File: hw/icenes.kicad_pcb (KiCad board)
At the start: 6 copper layers, 206 parts, among them J1 USB_B_Micro, J2 Barrel_Jack_Switch, J3 Conn_02x11_Odd_Even, J4 Conn_02x31_Odd_Even, J5 Conn_02x31_Odd_Even, J6 NES-Connector-72pin, U1 TPS62050, U10 74ALVC164245, U11 74ALVC164245, U12 74ALVC164245, U13 74ALVC164245, U2 TPS62050, U3 TPS62056, U4 iCE40HX8K-CT256, U5 93LC56C-I_SN, U6 FT2232H, U7 AT25SF041-SSHD, U8 SN74LVC1404, U9 SN74LVC1404, X1 DSC1001DI2-012.0000, X2 DSC1001BI2-133.0000T, Y1 21.47727MHz, Y2 26.601712MHz

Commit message: layout work.
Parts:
- C100, C101, C102, C103, C104, C105, C90, C91, C92, C93, C94, C95, C96, C97, C98, C99: moved to B.Cu
- moved R28 37.4 mm to (117.5, 115.5), turned to 270 degrees
- moved D3 37.4 mm to (117.5, 119.6), turned to 90 degrees
- moved R29 27.9 mm to (112.5, 115.5), turned to 270 degrees
- moved D10 27.7 mm to (82.5, 119.6), turned to 90 degrees
- moved R35 27.6 mm to (82.5, 115.5), turned to 270 degrees
- moved D4 27.6 mm to (112.5, 119.6), turned to 90 degrees
- moved D9 18.6 mm to (87.5, 119.6), turned to 90 degrees
- moved R30 18.5 mm to (107.5, 115.5), turned to 270 degrees
- moved R34 18.3 mm to (87.5, 115.5), turned to 270 degrees
- moved D5 18.2 mm to (107.5, 119.6), turned to 90 degrees
- moved R33 9.66 mm to (92.5, 115.5), turned to 270 degrees
- moved C101 9.54 mm to (71.8, 122.0)
- moved C102 9.54 mm to (66.2, 132.6)
- moved C104 9.54 mm to (71.8, 132.6)
- moved U13 9.54 mm to (69.8, 127.2)
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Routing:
- net GND: track 0.62 -> 0.00 mm, vias 0 -> 2
- net /ICENES io2/GPIO_J5: track 0.00 -> 0.62 mm
- net +1V8_FTDI: track 0.58 -> 0.00 mm

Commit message: Layout.
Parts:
- removed C74: C0.1uF, Capacitor_SMD:C_0603_1608Metric_Pad1.05x0.95mm_HandSolder
- removed D11: Green_LED, LED_SMD:LED_0805_2012Metric_Pad1.15x1.40mm_HandSolder
- removed R38: R0_0603, Resistor_SMD:R_0603_1608Metric_Pad1.05x0.95mm_HandSolder
- removed TP18: TestPoint, TestPoint:TestPoint_Pad_D1.0mm
- removed X2: DSC1001BI2-133.0000T, icenes-library:MEMS_Microship_Ocillator_SMD_CDFN-4_5.0x3.2mm
- C44, C46, C48, C49, C50, C52, C53, C58, C59, C61, C63, C65, C68, C72, C73, C75, C76, C79, C82, C86, C87: moved to B.Cu
- moved TP19 46.0 mm to (100.0, 90.5)
- moved R25 42.3 mm to (131.1, 100.0), turned to 90 degrees
- moved C56 42.0 mm to (130.2, 102.5)
- moved C55 42.0 mm to (130.1, 97.5)
- moved Y2 42.0 mm to (134.8, 97.5)
- moved C37 41.7 mm to (100.0, 84.6), turned to 180 degrees
- moved Y1 41.4 mm to (62.9, 97.6)
- moved X1 40.3 mm to (100.0, 86.9), turned to 180 degrees
- moved R22 35.4 mm to (66.5, 100.0), turned to 90 degrees
- moved C47 35.3 mm to (67.4, 97.5), turned to 0 degrees
- moved C51 35.3 mm to (67.4, 102.4), turned to 0 degrees
- moved R26 33.8 mm to (126.4, 98.5), turned to 90 degrees
- moved R27 31.9 mm to (124.8, 101.5)
- moved U9 29.2 mm to (123.3, 98.5), turned to 180 degrees
- moved R23 29.0 mm to (71.2, 101.5), turned to 270 degrees
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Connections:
- U4 pad K9: /ICENES io2/ICE_CLK_133MHz -> Net-(U4-PadK9)

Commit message: Layout.
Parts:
- C48, C49, C52, C59, C61, C63, C65, C68, C75, C79, C82, C87: moved to F.Cu
- moved C106 92.8 mm to (53.6, 141.5), turned to 90 degrees
- moved C103 40.2 mm to (132.1, 132.6)
- moved C100 40.2 mm to (133.8, 122.0)
- moved C105 40.2 mm to (126.5, 132.6)
- moved C98 40.2 mm to (128.2, 122.0)
- moved U12 40.2 mm to (130.2, 127.2)
- moved C95 20.2 mm to (111.9, 132.6)
- moved C96 20.2 mm to (91.8, 132.6)
- moved C97 20.2 mm to (106.3, 132.6)
- moved C94 20.1 mm to (86.2, 132.6)
- moved C91 20.1 mm to (86.3, 122.0)
- moved C93 20.1 mm to (91.8, 122.0)
- moved U10 20.1 mm to (110.0, 127.2)
- moved U11 20.1 mm to (90.0, 127.2)
- moved C92 20.0 mm to (106.5, 122.0)
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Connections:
- net USB_DM renamed USB_D_N
- net USB_DP renamed USB_D_P
- C60 pad 1: +5V -> +1V2
- C64 pad 1: +1V2 -> +5V
- C66 pad 1: +5V -> +1V2
- C67 pad 2: +5V -> +1V2
- C77 pad 1: +1V2 -> +5V
- C78 pad 2: +1V2 -> +5V
- C80 pad 1: +5V -> +1V2
- C81 pad 2: +5V -> +1V2
- C88 pad 1: +1V2 -> +5V
- C89 pad 2: +1V2 -> +5V
- J3 pad 1: +1V2 -> +5V
- J3 pad 5: +5V -> +1V2
- J4 pad 1: +1V2 -> +5V
- J4 pad 5: +5V -> +1V2
- J4 pad 57: +5V -> +1V2
- J4 pad 61: +1V2 -> +5V
- J5 pad 1: +1V2 -> +5V
- J5 pad 5: +5V -> +1V2
- J5 pad 57: +5V -> +1V2
- J5 pad 61: +1V2 -> +5V
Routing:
- net GND: track 0.00 -> 137.4 mm, vias 2 -> 47
- net +1V2: track 0.04 -> 107.1 mm, vias 0 -> 10
- net +3V3: track 0.00 -> 71.7 mm, vias 0 -> 22
- net +3V3_FTDI: track 0.00 -> 49.9 mm, vias 0 -> 10
- net ICE_CLK_12MHZ: track 0.00 -> 41.7 mm, vias 0 -> 2
- net +1V8_FTDI: track 0.00 -> 31.8 mm
- net Net-(L3-Pad2): track 0.00 -> 30.8 mm
- net Net-(C5-Pad2): track 0.00 -> 29.5 mm
- net Net-(C6-Pad2): track 0.00 -> 29.4 mm
- net USB_D_N: track 0.00 -> 27.5 mm, vias 0 -> 2
- net USB_D_P: track 0.00 -> 27.5 mm, vias 0 -> 2
- net Net-(R16-Pad2): track 0.00 -> 21.6 mm
- net /Vin(+5V-+10V): track 0.00 -> 18.8 mm, vias 0 -> 6
- net Net-(C6-Pad1): track 0.00 -> 18.1 mm
- net Net-(C5-Pad1): track 0.00 -> 18.1 mm
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- added copper zone on In4.Cu, net +1V2
- added copper zone on In4.Cu, net +3V3
- added copper zone on In4.Cu, net +3V3_FTDI
- added copper zone on In4.Cu, net +5V
- added copper zone on In4.Cu, net /Vin(+5V-+10V)
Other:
- board outline added: 100 x 100 mm
- net class Default: clearance 0.15 -> 0.127
- rule trace_clearance: 0.15 -> 0.127

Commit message: Layout.
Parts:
- moved C98 2.23 mm to (126.6, 123.5), turned to 0 degrees
- moved C100 2.22 mm to (132.2, 123.5), turned to 0 degrees
- moved C97 1.57 mm to (106.5, 131.0)
- moved C94 1.56 mm to (86.4, 131.0)
- moved C96 1.56 mm to (92.0, 131.0)
- moved C95 1.56 mm to (112.0, 131.0)
- moved C90 1.56 mm to (112.0, 123.5)
- moved C99 1.56 mm to (66.3, 123.5)
- moved C103 1.55 mm to (132.2, 131.0)
- moved C93 1.55 mm to (92.0, 123.5)
- moved C105 1.55 mm to (126.6, 131.0)
- moved C104 1.55 mm to (71.8, 131.0)
- moved C101 1.55 mm to (71.8, 123.5)
- moved C102 1.55 mm to (66.3, 131.0)
- moved C91 1.55 mm to (86.4, 123.5)
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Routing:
- net +1V2: track 107.1 -> 263.1 mm
- net /ICENES NES Connector/NES_SYSTEM_CLK: track 0.00 -> 118.6 mm
- net /ICENES NES Connector/NES_M2: track 0.00 -> 115.3 mm
- net GND: track 137.4 -> 239.9 mm, vias 47 -> 80
- net /ICENES NES Connector/~NES_ROMSEL: track 0.00 -> 86.4 mm
- net /ICENES NES Connector/NES_PPU_A10: track 0.00 -> 55.9 mm
- net /ICENES NES Connector/NES_PPU_A13: track 0.00 -> 54.7 mm
- net /ICENES NES Connector/NES_PPU_A12: track 0.00 -> 54.3 mm
- net /ICENES NES Connector/NES_PPU_A9: track 0.00 -> 52.4 mm
- net /ICENES NES Connector/NES_PPU_A8: track 0.00 -> 52.0 mm, vias 0 -> 1
- net /ICENES NES Connector/NES_PPU_A7: track 0.00 -> 51.6 mm, vias 0 -> 1
- net /ICENES NES Connector/NES_CPU_D7: track 0.00 -> 50.5 mm, vias 0 -> 1
- net /ICENES NES Connector/NES_CPU_D6: track 0.00 -> 48.4 mm, vias 0 -> 1
- net /ICENES NES Connector/~NES_IRQ: track 0.00 -> 48.2 mm, vias 0 -> 1
- net /ICENES NES Connector/NES_CPU_D5: track 0.00 -> 47.8 mm, vias 0 -> 1
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
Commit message: Layout.
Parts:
- turned U4 to 180 degrees
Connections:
- U4 pad F7: /ICENES io1/ICE_CLK_21.47727MHz -> /ICENES io1/ICE_CLK_26.601712MHz
- U4 pad H16: /ICENES io1/ICE_CLK_26.601712MHz -> /ICENES io1/ICE_CLK_21.47727MHz
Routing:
- net ICE_CLK_12MHZ: track 41.7 -> 51.8 mm, vias 2 -> 3
- net /ICENES io1/ICE_CLK_26.601712MHz: track 2.35 -> 9.84 mm
- net /ICENES io2/GPIO_H5: track 0.57 -> 7.20 mm
- net /ICENES io2/GPIO_L7: track 0.57 -> 7.06 mm
- net /ICENES io2/GPIO_H6: track 0.57 -> 7.03 mm
- net /ICENES io2/GPIO_K5: track 0.57 -> 6.43 mm
- net /ICENES io1/GPIO_G11: track 0.57 -> 6.40 mm
- net ICE_SYSTEM_CLK: track 0.57 -> 6.23 mm
- net ~ICE_PPU_A13: track 0.57 -> 6.23 mm
- net /ICENES io2/GPIO_G5: track 0.57 -> 6.23 mm
- net /ICENES io1/GPIO_G10: track 0.57 -> 6.23 mm
- net /ICENES io1/LED1: track 1.59 -> 7.13 mm
- net DSRn: track 0.57 -> 6.02 mm, vias 1 -> 2
- net /ICENES io2/GPIO_L9: track 0.57 -> 5.60 mm
- net ~CPU_DATA_OE: track 0.57 -> 5.59 mm
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
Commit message: Layout.
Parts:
- moved C65 81.3 mm to (170.7, 84.4)
- moved C68 81.3 mm to (170.6, 88.4)
- moved C75 81.3 mm to (170.6, 92.4)
- moved C63 72.4 mm to (166.5, 93.3), turned to 0 degrees
- moved C59 69.5 mm to (166.5, 89.3), turned to 0 degrees
- moved C61 66.6 mm to (166.5, 84.5), turned to 0 degrees
- moved C82 63.9 mm to (158.6, 93.1), turned to 0 degrees
- moved C79 62.2 mm to (158.6, 91.5), turned to 0 degrees
- moved C87 56.1 mm to (158.7, 85.1), turned to 0 degrees
- moved C48 54.1 mm to (162.8, 93.3)
- moved C49 54.1 mm to (162.8, 88.8)
- moved C52 54.1 mm to (162.8, 84.8)
- moved R37 18.7 mm to (94.0, 86.3), turned to 270 degrees
- moved TP17 17.6 mm to (94.0, 89.2)
- moved TP16 17.1 mm to (97.0, 89.2)
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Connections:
- J3 pad 10: /ICENES io1/GPIO_G14 -> Net-(J3-Pad10)
- J3 pad 11: /ICENES io1/GPIO_G10 -> Net-(J3-Pad11)
- J3 pad 12: /ICENES io1/GPIO_E16 -> Net-(J3-Pad12)
- J3 pad 13: /ICENES io1/GPIO_G15 -> Net-(J3-Pad13)
- J3 pad 14: /ICENES io1/GPIO_G13 -> Net-(J3-Pad14)
- J3 pad 15: /ICENES io1/GPIO_H12 -> Net-(J3-Pad15)
- J3 pad 16: /ICENES io1/GPIO_D16 -> Net-(J3-Pad16)
- J3 pad 17: /ICENES io1/GPIO_G16 -> Net-(J3-Pad17)
- J3 pad 18: /ICENES io1/GPIO_G12 -> Net-(J3-Pad18)
- J3 pad 19: /ICENES io1/GPIO_H14 -> Net-(J3-Pad19)
- J3 pad 20: /ICENES io1/GPIO_F14 -> Net-(J3-Pad20)
- J3 pad 21: /ICENES io1/GPIO_H13 -> Net-(J3-Pad21)
- J3 pad 22: /ICENES io1/GPIO_F12 -> Net-(J3-Pad22)
- J3 pad 7: /ICENES io1/GPIO_G11 -> Net-(J3-Pad7)
- J3 pad 8: /ICENES io1/GPIO_F15 -> Net-(J3-Pad8)
- J3 pad 9: /ICENES io1/GPIO_F16 -> Net-(J3-Pad9)
- J4 pad 10: /ICENES io2/GPIO_M9 -> Net-(J4-Pad10)
- J4 pad 11: /ICENES io2/GPIO_P4 -> Net-(J4-Pad11)
- J4 pad 12: /ICENES io2/GPIO_P9 -> Net-(J4-Pad12)
- J4 pad 13: /ICENES io2/GPIO_R2 -> Net-(J4-Pad13)
- J4 pad 14: /ICENES io2/GPIO_R10 -> Net-(J4-Pad14)
- J4 pad 15: /ICENES io2/GPIO_N5 -> Net-(J4-Pad15)
- J4 pad 16: /ICENES io2/GPIO_L10 -> Net-(J4-Pad16)
- J4 pad 17: /ICENES io2/GPIO_T2 -> Net-(J4-Pad17)
- J4 pad 18: /ICENES io2/GPIO_P10 -> Net-(J4-Pad18)
- J4 pad 19: /ICENES io2/GPIO_P5 -> Net-(J4-Pad19)
- J4 pad 20: /ICENES io2/GPIO_N10 -> Net-(J4-Pad20)
- J4 pad 21: /ICENES io2/GPIO_R3 -> Net-(J4-Pad21)
- J4 pad 22: /ICENES io2/GPIO_T10 -> Net-(J4-Pad22)
- J4 pad 23: /ICENES io2/GPIO_R5 -> Net-(J4-Pad23)
- J4 pad 24: /ICENES io2/GPIO_T11 -> Net-(J4-Pad24)
- J4 pad 25: /ICENES io2/GPIO_T3 -> Net-(J4-Pad25)
- J4 pad 26: /ICENES io2/GPIO_T15 -> Net-(J4-Pad26)
- J4 pad 27: /ICENES io2/GPIO_R4 -> Net-(J4-Pad27)
- J4 pad 28: /ICENES io2/GPIO_T14 -> Net-(J4-Pad28)
- J4 pad 29: /ICENES io2/GPIO_M7 -> Net-(J4-Pad29)
- J4 pad 30: /ICENES io2/GPIO_M11 -> Net-(J4-Pad30)
- J4 pad 33: /ICENES io2/GPIO_N7 -> Net-(J4-Pad33)
- J4 pad 35: /ICENES io2/GPIO_P6 -> Net-(J4-Pad35)
- J4 pad 36: /ICENES io2/GPIO_T13 -> Net-(J4-Pad36)
- J4 pad 37: /ICENES io2/GPIO_M8 -> Net-(J4-Pad37)
- J4 pad 38: /ICENES io2/GPIO_N12 -> Net-(J4-Pad38)
- J4 pad 39: /ICENES io2/GPIO_T5 -> Net-(J4-Pad39)
- J4 pad 40: /ICENES io2/GPIO_L11 -> Net-(J4-Pad40)
- J4 pad 41: /ICENES io2/GPIO_R6 -> Net-(J4-Pad41)
- J4 pad 42: /ICENES io2/GPIO_T16 -> Net-(J4-Pad42)
- J4 pad 43: /ICENES io2/GPIO_P8 -> Net-(J4-Pad43)
- J4 pad 44: /ICENES io2/GPIO_M12 -> Net-(J4-Pad44)
- J4 pad 45: /ICENES io2/GPIO_T6 -> Net-(J4-Pad45)
- J4 pad 46: /ICENES io2/GPIO_R16 -> Net-(J4-Pad46)
- J4 pad 47: /ICENES io2/GPIO_L9 -> Net-(J4-Pad47)
- J4 pad 48: /ICENES io2/GPIO_K11 -> Net-(J4-Pad48)
- J4 pad 49: /ICENES io2/GPIO_T7 -> Net-(J4-Pad49)
- J4 pad 50: /ICENES io2/GPIO_P13 -> Net-(J4-Pad50)
- J4 pad 51: /ICENES io2/GPIO_T8 -> Net-(J4-Pad51)
- J4 pad 52: /ICENES io2/GPIO_M5 -> Net-(J4-Pad52)
- J4 pad 53: /ICENES io2/GPIO_P7 -> Net-(J4-Pad53)
- J4 pad 54: /ICENES io2/GPIO_R1 -> Net-(J4-Pad54)
- J4 pad 55: /ICENES io2/GPIO_N9 -> Net-(J4-Pad55)
- J4 pad 56: /ICENES io2/GPIO_N4 -> Net-(J4-Pad56)
- J4 pad 7: /ICENES io2/GPIO_N6 -> Net-(J4-Pad7)
- J4 pad 8: /ICENES io2/GPIO_T9 -> Net-(J4-Pad8)
- J4 pad 9: /ICENES io2/GPIO_T1 -> Net-(J4-Pad9)
- J5 pad 10: /ICENES io2/GPIO_H1 -> Net-(J5-Pad10)
- J5 pad 11: /ICENES io2/GPIO_F5 -> Net-(J5-Pad11)
- J5 pad 12: /ICENES io2/GPIO_J2 -> Net-(J5-Pad12)
- J5 pad 13: /ICENES io2/GPIO_B1 -> Net-(J5-Pad13)
- J5 pad 14: /ICENES io2/GPIO_J1 -> Net-(J5-Pad14)
- J5 pad 15: /ICENES io2/GPIO_C1 -> Net-(J5-Pad15)
- J5 pad 16: /ICENES io2/GPIO_K1 -> Net-(J5-Pad16)
- J5 pad 17: /ICENES io2/GPIO_C2 -> Net-(J5-Pad17)
- J5 pad 18: /ICENES io2/GPIO_K3 -> Net-(J5-Pad18)
- J5 pad 19: /ICENES io2/GPIO_F4 -> Net-(J5-Pad19)
- J5 pad 20: /ICENES io2/GPIO_L4 -> Net-(J5-Pad20)
- J5 pad 21: /ICENES io2/GPIO_D2 -> Net-(J5-Pad21)
- J5 pad 22: /ICENES io2/GPIO_L1 -> Net-(J5-Pad22)
- J5 pad 23: /ICENES io2/GPIO_G5 -> Net-(J5-Pad23)
- J5 pad 24: /ICENES io2/GPIO_K4 -> Net-(J5-Pad24)
- J5 pad 25: /ICENES io2/GPIO_D1 -> Net-(J5-Pad25)
- J5 pad 26: /ICENES io2/GPIO_M1 -> Net-(J5-Pad26)
- J5 pad 27: /ICENES io2/GPIO_G4 -> Net-(J5-Pad27)
- J5 pad 28: /ICENES io2/GPIO_L6 -> Net-(J5-Pad28)
- J5 pad 29: /ICENES io2/GPIO_E3 -> Net-(J5-Pad29)
- J5 pad 30: /ICENES io2/GPIO_L3 -> Net-(J5-Pad30)
- J5 pad 33: /ICENES io2/GPIO_H5 -> Net-(J5-Pad33)
- J5 pad 35: /ICENES io2/GPIO_E2 -> Net-(J5-Pad35)
- J5 pad 36: /ICENES io2/GPIO_K5 -> Net-(J5-Pad36)
- J5 pad 37: /ICENES io2/GPIO_G3 -> Net-(J5-Pad37)
- J5 pad 38: /ICENES io2/GPIO_M2 -> Net-(J5-Pad38)
- J5 pad 39: /ICENES io2/GPIO_F3 -> Net-(J5-Pad39)
- J5 pad 40: /ICENES io2/GPIO_L7 -> Net-(J5-Pad40)
- J5 pad 41: /ICENES io2/GPIO_H3 -> Net-(J5-Pad41)
- J5 pad 42: /ICENES io2/GPIO_N2 -> Net-(J5-Pad42)
- J5 pad 43: /ICENES io2/GPIO_F2 -> Net-(J5-Pad43)
- J5 pad 44: /ICENES io2/GPIO_M6 -> Net-(J5-Pad44)
- J5 pad 45: /ICENES io2/GPIO_H6 -> Net-(J5-Pad45)
- J5 pad 46: /ICENES io2/GPIO_M3 -> Net-(J5-Pad46)
- J5 pad 47: /ICENES io2/GPIO_F1 -> Net-(J5-Pad47)
- J5 pad 48: /ICENES io2/GPIO_L5 -> Net-(J5-Pad48)
- J5 pad 49: /ICENES io2/GPIO_H4 -> Net-(J5-Pad49)
- J5 pad 50: /ICENES io2/GPIO_N3 -> Net-(J5-Pad50)
- J5 pad 51: /ICENES io2/GPIO_G2 -> Net-(J5-Pad51)
- J5 pad 52: /ICENES io2/GPIO_P1 -> Net-(J5-Pad52)
- J5 pad 53: /ICENES io2/GPIO_J4 -> Net-(J5-Pad53)
- J5 pad 54: /ICENES io2/GPIO_M4 -> Net-(J5-Pad54)
- J5 pad 55: /ICENES io2/GPIO_H2 -> Net-(J5-Pad55)
- J5 pad 56: /ICENES io2/GPIO_P2 -> Net-(J5-Pad56)
- J5 pad 7: /ICENES io2/GPIO_E4 -> Net-(J5-Pad7)
- J5 pad 8: /ICENES io2/GPIO_J5 -> Net-(J5-Pad8)
- J5 pad 9: /ICENES io2/GPIO_B2 -> Net-(J5-Pad9)
- U4 pad A1: ICE_CPU_A0 -> ICE_CPU_RW
- U4 pad A10: ICE_PPU_A7 -> ICE_PPU_A9
- U4 pad A11: ICE_PPU_A8 -> ICE_PPU_A7
- U4 pad A15: PPU_ADDR_DIR -> ICE_PPU_D7
- U4 pad A16: ~PPU_ADDR_OE -> ICE_PPU_D6
- U4 pad A2: ICE_CPU_A2 -> ICE_CPU_A13
- U4 pad A5: ICE_CPU_A6 -> ICE_CPU_A9
- U4 pad A6: ICE_CPU_A8 -> ICE_CPU_A7
- U4 pad A7: ICE_CPU_A14 -> ICE_CPU_A3
- U4 pad B10: ICE_PPU_A4 -> ICE_PPU_A8
- U4 pad B11: ICE_PPU_A5 -> ICE_PPU_A1
- U4 pad B12: ICE_PPU_A3 -> ICE_PPU_A0
- U4 pad B13: ~ICE_PPU_WR -> PPU_DATA_DIR
- U4 pad B14: CTSn -> ~PPU_DATA_OE
- U4 pad B15: RS232_TX_TTL -> ICE_PPU_D0
- U4 pad B16: /ICENES io1/LED5 -> ICE_CPU_D7
- U4 pad B3: ICE_PPU_D7 -> ICE_CPU_A8
- U4 pad B4: ICE_CPU_A3 -> ICE_CPU_A12
- U4 pad B5: ICE_CPU_A5 -> ICE_CPU_A10
- U4 pad B6: ICE_CPU_A11 -> ICE_CPU_A4
- U4 pad B7: ICE_CPU_A12 -> ICE_CPU_A1
- U4 pad B8: ICE_CPU_RW -> ICE_CPU_A0
- U4 pad B9: ~CPU_ADDR_OE -> ICE_PPU_A11
- U4 pad C11: ICE_PPU_A1 -> ICE_PPU_A5
- U4 pad C12: DTRn -> ~PPU_ADDR_OE
- U4 pad C13: DCDn -> PPU_ADDR_DIR
- U4 pad C14: RS232_RX_TTL -> ICE_PPU_D1
- U4 pad C16: /ICENES io1/LED3 -> ICE_CPU_D6
- U4 pad C3: ICE_PPU_D3 -> ICE_CPU_A11
- U4 pad C4: CPU_DATA_DIR -> ICE_CPU_A6
- U4 pad C5: ~PPU_DATA_OE -> ICE_CPU_A5
- U4 pad C6: ICE_CPU_A10 -> ~CPU_ADDR_OE
- U4 pad C7: ICE_CPU_A13 -> ~ICE_PPU_WR
- U4 pad C8: PPU_DATA_DIR -> ~ICE_PPU_A13
- U4 pad D10: ICE_PPU_A9 -> /ICENES io1/LED4
- U4 pad D11: ICE_PPU_A2 -> /ICENES io1/LED3
- U4 pad D13: RTSn -> /ICENES io1/LED1
- U4 pad D14: /ICENES io1/LED7 -> ICE_CPU_D4
- U4 pad D15: /ICENES io1/LED0 -> ICE_CPU_D5
- U4 pad D16: /ICENES io1/GPIO_D16 -> ICE_CPU_D2
- U4 pad D3: ICE_PPU_D4 -> ICE_CPU_A14
- U4 pad D4: ICE_PPU_D6 -> /ICENES io1/LED7
- U4 pad D5: ICE_CPU_A1 -> /ICENES io1/LED6
- U4 pad D6: ICE_CPU_A7 -> ICE_CPU_A2
- U4 pad D7: ICE_CPU_A9 -> CPU_ADDR_DIR
- U4 pad D8: CPU_ADDR_DIR -> ICE_PPU_A3
- U4 pad E10: ICE_PPU_A0 -> ICE_PPU_D4
- U4 pad E11: DSRn -> /ICENES io1/LED2
- U4 pad E13: /ICENES io1/LED6 -> ICE_CICtoMB
- U4 pad E14: /ICENES io1/LED2 -> ICE_CPU_D3
- U4 pad E16: /ICENES io1/GPIO_E16 -> ICE_CPU_D1
- U4 pad E5: ICE_PPU_D5 -> /ICENES io1/LED5
- U4 pad E6: ICE_CPU_A4 -> ICE_PPU_A4
- U4 pad E9: ICE_PPU_A11 -> ICE_PPU_A2
- U4 pad F11: /ICENES io1/LED1 -> /ICENES io1/LED0
- U4 pad F12: /ICENES io1/GPIO_F12 -> ICE_M2
- U4 pad F13: /ICENES io1/LED4 -> ~ICE_CIC_RST
- U4 pad F14: /ICENES io1/GPIO_F14 -> CPU_DATA_DIR
- U4 pad F15: /ICENES io1/GPIO_F15 -> ICE_CIRAM_A10
- U4 pad F16: /ICENES io1/GPIO_F16 -> ICE_CPU_D0
- U4 pad F9: ~ICE_PPU_A13 -> ICE_PPU_D5
- U4 pad G10: /ICENES io1/GPIO_G10 -> ICE_PPU_D3
- U4 pad G11: /ICENES io1/GPIO_G11 -> ICE_PPU_D2
- U4 pad G12: /ICENES io1/GPIO_G12 -> ICE_SYSTEM_CLK
- U4 pad G13: /ICENES io1/GPIO_G13 -> ICE_CICtoPak
- U4 pad G15: /ICENES io1/GPIO_G15 -> ~ICE_CIRAM_CE
- U4 pad G16: /ICENES io1/GPIO_G16 -> ~CPU_DATA_OE
- U4 pad H11: ~CPU_DATA_OE -> /ICENES io1/GPIO_H11
- U4 pad H12: /ICENES io1/GPIO_H12 -> /ICENES io1/GPIO_E13
- U4 pad H13: /ICENES io1/GPIO_H13 -> ICE_CIC_CLK
- U4 pad H14: /ICENES io1/GPIO_H14 -> ~ICE_IRQ
- U4 pad J10: ICE_SYSTEM_CLK -> /ICENES io1/GPIO_C10
- U4 pad J11: ~ICE_PPU_RD -> /ICENES io1/GPIO_J11
- U4 pad J12: ~ICE_IRQ -> /ICENES io1/GPIO_J12
- U4 pad J13: ~ICE_CIRAM_CE -> /ICENES io1/GPIO_J13
- U4 pad J14: ICE_CICtoMB -> /ICENES io1/GPIO_J14
- U4 pad J15: ~ICE_CIC_RST -> ~MISC_OE2
- U4 pad J16: ICE_CIRAM_A10 -> MISC_DIR2
- U4 pad K12: ~MISC_OE1 -> /ICENES io1/GPIO_K12
- U4 pad K13: ICE_CIC_CLK -> /ICENES io1/GPIO_K13
- U4 pad K14: ICE_CICtoPak -> /ICENES io1/GPIO_K14
- U4 pad K15: ~MISC_OE2 -> ~ICE_PPU_RD
- U4 pad K16: MISC_DIR2 -> ~ICE_ROMSEL
- U4 pad L12: ICE_CPU_D3 -> /ICENES io1/GPIO_L12
- U4 pad L13: ICE_CPU_D1 -> /ICENES io1/GPIO_L13
- U4 pad L14: ICE_CPU_D0 -> /ICENES io1/GPIO_M16
- U4 pad L16: ~ICE_ROMSEL -> ~MISC_OE1
- U4 pad M13: ICE_CPU_D5 -> /ICENES io1/GPIO_M13
- U4 pad M14: ICE_CPU_D4 -> /ICENES io1/GPIO_M14
- U4 pad M15: ICE_M2 -> /ICENES io1/GPIO_M15
- U4 pad N10: /ICENES io2/GPIO_N10 -> RTSn
- U4 pad N16: ICE_CPU_D2 -> /ICENES io1/GPIO_N16
- U4 pad N9: /ICENES io2/GPIO_N9 -> DTRn
- U4 pad P10: /ICENES io2/GPIO_P10 -> CTSn
- U4 pad P14: ICE_PPU_D0 -> /ICENES io1/GPIO_P14
- U4 pad P15: ICE_CPU_D7 -> /ICENES io1/GPIO_P15
- U4 pad P16: ICE_CPU_D6 -> /ICENES io1/GPIO_P16
- U4 pad P8: /ICENES io2/GPIO_P8 -> DCDn
- U4 pad P9: /ICENES io2/GPIO_P9 -> DSRn
- U4 pad R10: /ICENES io2/GPIO_R10 -> RS232_TX_TTL
- U4 pad R14: ICE_PPU_D2 -> /ICENES io1/GPIO_R14
- U4 pad R15: ICE_PPU_D1 -> /ICENES io1/GPIO_R15
- U4 pad T10: /ICENES io2/GPIO_T10 -> RS232_RX_TTL
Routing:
- net MISC_DIR1: track 0.85 -> 49.5 mm
- net ~CPU_ADDR_OE: track 2.02 -> 49.9 mm, vias 0 -> 3
- net CPU_ADDR_DIR: track 17.8 -> 60.6 mm
- net ICE_M2: track 1.87 -> 42.2 mm, vias 0 -> 2
- net ICE_CPU_A14: track 1.00 -> 40.9 mm, vias 0 -> 2
- net MISC_DIR2: track 0.90 -> 39.7 mm
- net ICE_CPU_A12: track 2.02 -> 39.9 mm
- net ICE_CPU_A0: track 1.05 -> 38.8 mm
- net ~MISC_OE1: track 4.63 -> 42.2 mm, vias 1 -> 0
- net ICE_CPU_A2: track 1.05 -> 38.6 mm, vias 0 -> 2
- net ICE_CPU_A6: track 1.05 -> 38.2 mm, vias 0 -> 2
- net ICE_CPU_A3: track 1.97 -> 39.0 mm
- net ICE_CPU_A11: track 2.09 -> 39.1 mm, vias 0 -> 2
- net ICE_CPU_A10: track 2.87 -> 39.9 mm, vias 1 -> 0
- net ICE_SYSTEM_CLK: track 6.23 -> 43.1 mm, vias 1 -> 2
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
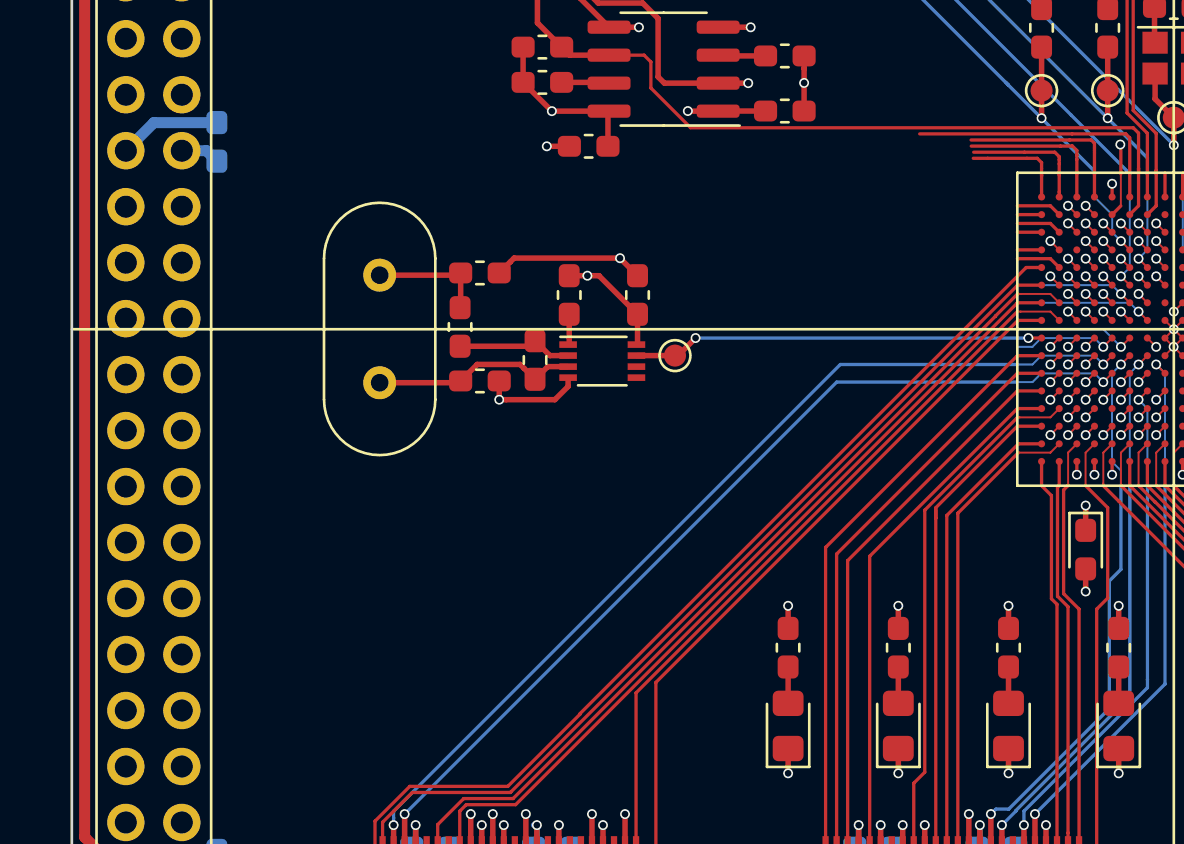
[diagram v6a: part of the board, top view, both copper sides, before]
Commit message: Layout. Added some info for the PAL crystal.
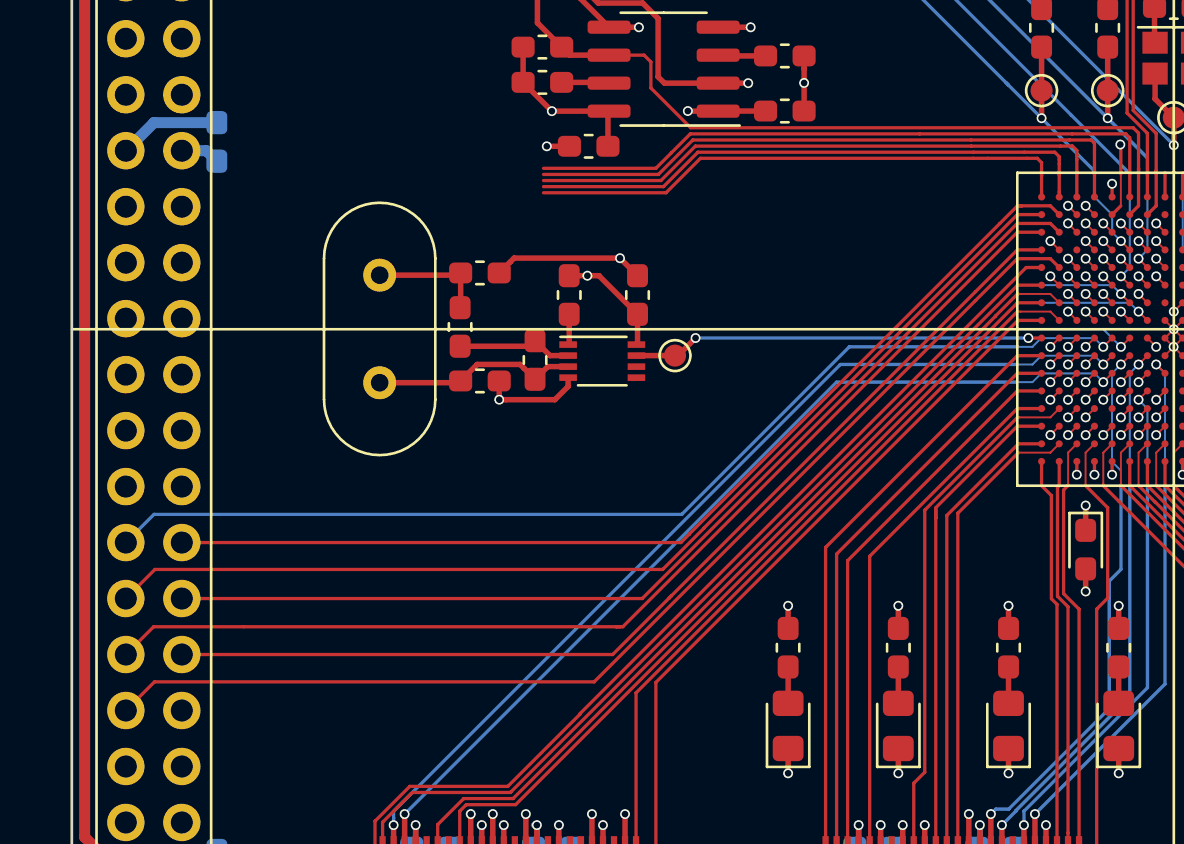
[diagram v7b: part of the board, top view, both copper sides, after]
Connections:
- J4 pad 33: Net-(J4-Pad33) -> GPIO_R14
- J4 pad 35: Net-(J4-Pad35) -> GPIO_P14
- J4 pad 36: Net-(J4-Pad36) -> /ICENES io2/GPIO_P13
- J4 pad 37: Net-(J4-Pad37) -> GPIO_M13
- J4 pad 38: Net-(J4-Pad38) -> /ICENES io2/GPIO_N12
- J4 pad 39: Net-(J4-Pad39) -> GPIO_L14
- J4 pad 40: Net-(J4-Pad40) -> GPIO_M14
- J4 pad 41: Net-(J4-Pad41) -> GPIO_K14
- J4 pad 42: Net-(J4-Pad42) -> GPIO_K13
- J4 pad 43: Net-(J4-Pad43) -> GPIO_J14
- J4 pad 44: Net-(J4-Pad44) -> GPIO_J13
- J4 pad 45: Net-(J4-Pad45) -> GPIO_R15
- J4 pad 46: Net-(J4-Pad46) -> GPIO_H12
- J4 pad 47: Net-(J4-Pad47) -> GPIO_P15
- J4 pad 48: Net-(J4-Pad48) -> /ICENES io2/GPIO_R16
- J4 pad 49: Net-(J4-Pad49) -> GPIO_N16
- J4 pad 50: Net-(J4-Pad50) -> GPIO_P16
- J4 pad 51: Net-(J4-Pad51) -> GPIO_L12
- J4 pad 52: Net-(J4-Pad52) -> GPIO_M15
- J4 pad 53: Net-(J4-Pad53) -> GPIO_K12
- J4 pad 54: Net-(J4-Pad54) -> GPIO_L13
- J4 pad 55: Net-(J4-Pad55) -> GPIO_J11
- J4 pad 56: Net-(J4-Pad56) -> GPIO_J12
- U4 pad H12: /ICENES io1/GPIO_E13 -> GPIO_H12
- U4 pad J11: /ICENES io1/GPIO_J11 -> GPIO_J11
- U4 pad J12: /ICENES io1/GPIO_J12 -> GPIO_J12
- U4 pad J13: /ICENES io1/GPIO_J13 -> GPIO_J13
- U4 pad J14: /ICENES io1/GPIO_J14 -> GPIO_J14
- U4 pad K12: /ICENES io1/GPIO_K12 -> GPIO_K12
- U4 pad K13: /ICENES io1/GPIO_K13 -> GPIO_K13
- U4 pad K14: /ICENES io1/GPIO_K14 -> GPIO_K14
- U4 pad L12: /ICENES io1/GPIO_L12 -> GPIO_L12
- U4 pad L13: /ICENES io1/GPIO_L13 -> GPIO_L13
- U4 pad L14: /ICENES io1/GPIO_M16 -> GPIO_L14
- U4 pad M13: /ICENES io1/GPIO_M13 -> GPIO_M13
- U4 pad M14: /ICENES io1/GPIO_M14 -> GPIO_M14
- U4 pad M15: /ICENES io1/GPIO_M15 -> GPIO_M15
- U4 pad N16: /ICENES io1/GPIO_N16 -> GPIO_N16
- U4 pad P14: /ICENES io1/GPIO_P14 -> GPIO_P14
- U4 pad P15: /ICENES io1/GPIO_P15 -> GPIO_P15
- U4 pad P16: /ICENES io1/GPIO_P16 -> GPIO_P16
- U4 pad R14: /ICENES io1/GPIO_R14 -> GPIO_R14
- U4 pad R15: /ICENES io1/GPIO_R15 -> GPIO_R15
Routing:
- net GPIO_J12: track 0.00 -> 54.5 mm, vias 0 -> 1
- net GPIO_L13: track 0.00 -> 53.3 mm, vias 0 -> 1
- net GPIO_J11: track 0.00 -> 52.8 mm, vias 0 -> 1
- net GPIO_M15: track 0.00 -> 52.5 mm
- net GPIO_K12: track 0.00 -> 51.4 mm, vias 0 -> 1
- net GPIO_L12: track 0.00 -> 50.9 mm, vias 0 -> 1
- net GPIO_P16: track 0.00 -> 49.7 mm
- net GPIO_H12: track 0.00 -> 48.9 mm, vias 0 -> 1
- net GPIO_N16: track 0.00 -> 47.9 mm
- net GPIO_J13: track 0.00 -> 47.7 mm, vias 0 -> 1
- net /ICENES io2/GPIO_R16: track 1.10 -> 48.8 mm
- net GPIO_K13: track 0.00 -> 47.3 mm, vias 0 -> 1
- net GPIO_P15: track 0.00 -> 47.0 mm
- net GPIO_R15: track 0.00 -> 46.5 mm
- net GPIO_M14: track 0.00 -> 45.5 mm, vias 0 -> 1
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
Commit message: Layout.
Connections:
- J4 pad 20: Net-(J4-Pad20) -> /ICENES io2/GPIO_M9
- J4 pad 21: Net-(J4-Pad21) -> /ICENES io2/GPIO_L9
- J4 pad 22: Net-(J4-Pad22) -> /ICENES io2/GPIO_L10
- J4 pad 23: Net-(J4-Pad23) -> /ICENES io2/GPIO_M11
- J4 pad 24: Net-(J4-Pad24) -> /ICENES io2/GPIO_M12
- J4 pad 25: Net-(J4-Pad25) -> /ICENES io2/GPIO_T11
- J4 pad 26: Net-(J4-Pad26) -> /ICENES io2/GPIO_L11
- J4 pad 27: Net-(J4-Pad27) -> /ICENES io2/GPIO_T14
- J4 pad 28: Net-(J4-Pad28) -> /ICENES io2/GPIO_T13
- J4 pad 29: Net-(J4-Pad29) -> /ICENES io2/GPIO_T16
- J4 pad 30: Net-(J4-Pad30) -> /ICENES io2/GPIO_T15
- U4 pad N10: RTSn -> DTRn
- U4 pad N9: DTRn -> DCDn
- U4 pad P10: CTSn -> DSRn
- U4 pad P8: DCDn -> /ICENES io2/GPIO_P8
- U4 pad P9: DSRn -> /ICENES io2/GPIO_P9
- U4 pad T8: /ICENES io2/GPIO_T8 -> CTSn
- U4 pad T9: /ICENES io2/GPIO_T9 -> RTSn
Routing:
- net /ICENES io2/GPIO_M9: track 10.1 -> 57.4 mm
- net /ICENES io2/GPIO_L10: track 8.51 -> 55.7 mm
- net /ICENES io2/GPIO_M12: track 4.63 -> 51.2 mm
- net /ICENES io2/GPIO_M11: track 6.11 -> 50.6 mm
- net /ICENES io2/GPIO_L9: track 9.76 -> 54.1 mm
- net /ICENES io2/GPIO_L11: track 26.0 -> 56.2 mm
- net /ICENES io2/GPIO_T13: track 29.2 -> 48.0 mm
- net /ICENES io2/GPIO_T11: track 30.0 -> 48.7 mm
- net /ICENES io2/GPIO_T15: track 26.8 -> 45.3 mm
- net /ICENES io2/GPIO_T14: track 28.1 -> 43.6 mm
- net /ICENES io2/GPIO_T16: track 25.9 -> 40.9 mm
- net DTRn: track 29.8 -> 33.8 mm
- net RS232_TX_TTL: track 30.9 -> 27.2 mm
- net /ICENES io2/GPIO_P9: track 0.00 -> 3.03 mm, vias 0 -> 1
- net /ICENES io2/GPIO_P8: track 0.00 -> 3.03 mm, vias 0 -> 1
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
